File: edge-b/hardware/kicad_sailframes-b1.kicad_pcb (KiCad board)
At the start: 2 copper layers, 80 x 56 mm, 0 parts

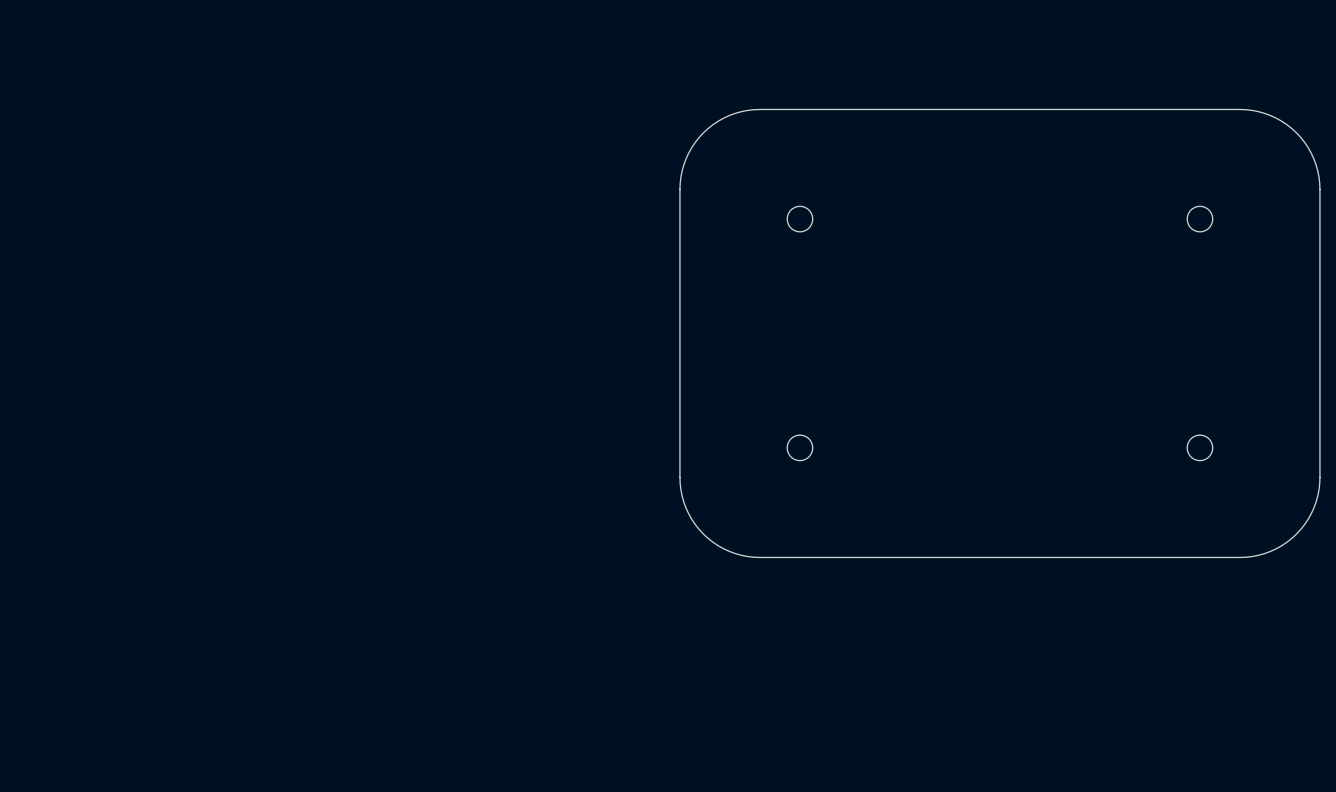
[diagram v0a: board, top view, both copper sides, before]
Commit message: B1 PCB v0.12: portrait rounded rectangle with top+bottom cut for expansion space
Final PCB outline:
- 79.3 x 73.9 mm rounded rectangle (R.377 on all 4 corners)
- Top and bottom cut symmetrically from original 104.7 mm Polycase template,
  leaving ~15.4 mm clear at each end for future expansion PCBs (GNSS antenna
  above the main PCB; spare module space below)
- 4 mounting holes at 2.375" (60.325 mm) X spacing, page-6 inner Y heights:
    (109.49, 76.97), (169.81, 76.97), (109.49, 126.98), (169.81, 126.98)
- Discards the page-6 corner-ear/cutout features since cuts remove the
  corners; portrait orientation matches installed pose (long axis vertical)

Co-Authored-By: Claude Opus 4.7 (1M context) <noreply@anthropic.com>
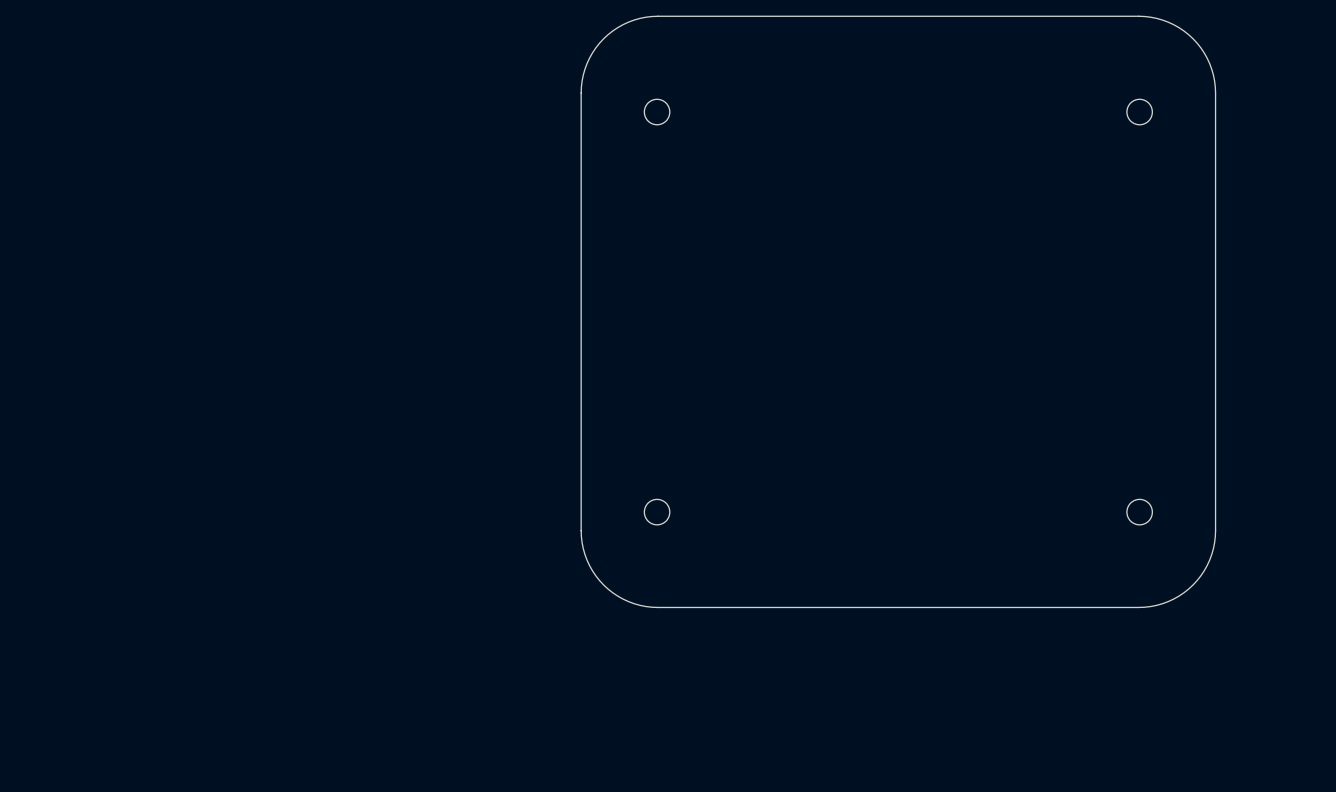
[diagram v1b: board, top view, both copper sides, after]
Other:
- board size 80 x 56 mm -> 79.3 x 73.9 mm
- board text added: "B1 PCB outline v0.5 — full Polycase ML-34BF-PCB template Envelope: 104.7 x 79.3 mm with 4x R.377 (9.6 mm) outer corners 4 edge notches centered on each side (R.125 / 3.18 mm inside fillets) Top/bottom notches: 73.9 mm wide x 9.6 mm deep Left/right notches: 46.6 mm wide x 9.6 mm deep 8 mounting holes NPTH 3.18 mm: 4 outer @ 85 x 60.3 mm, 4 inner @ 50 x 28.6 mm GNSS antenna NOT on main PCB (separat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"
- board text removed: "B1 PCB outline v0.4 — Option B: small centered rectangle 80 x 56 mm centered on Polycase interior, R=10 mm corner fillets 4 mounting holes NPTH 3.18 mm at +/-(25, 14.3) mm from Polycase center (inner PCB-mounting boss positions, 50 x 28.6 mm pattern) Clears 4 corner brass-insert towers laterally (no cover-screw holes through PCB) Cover screws engage corner brass inserts independently of PCB Anten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"

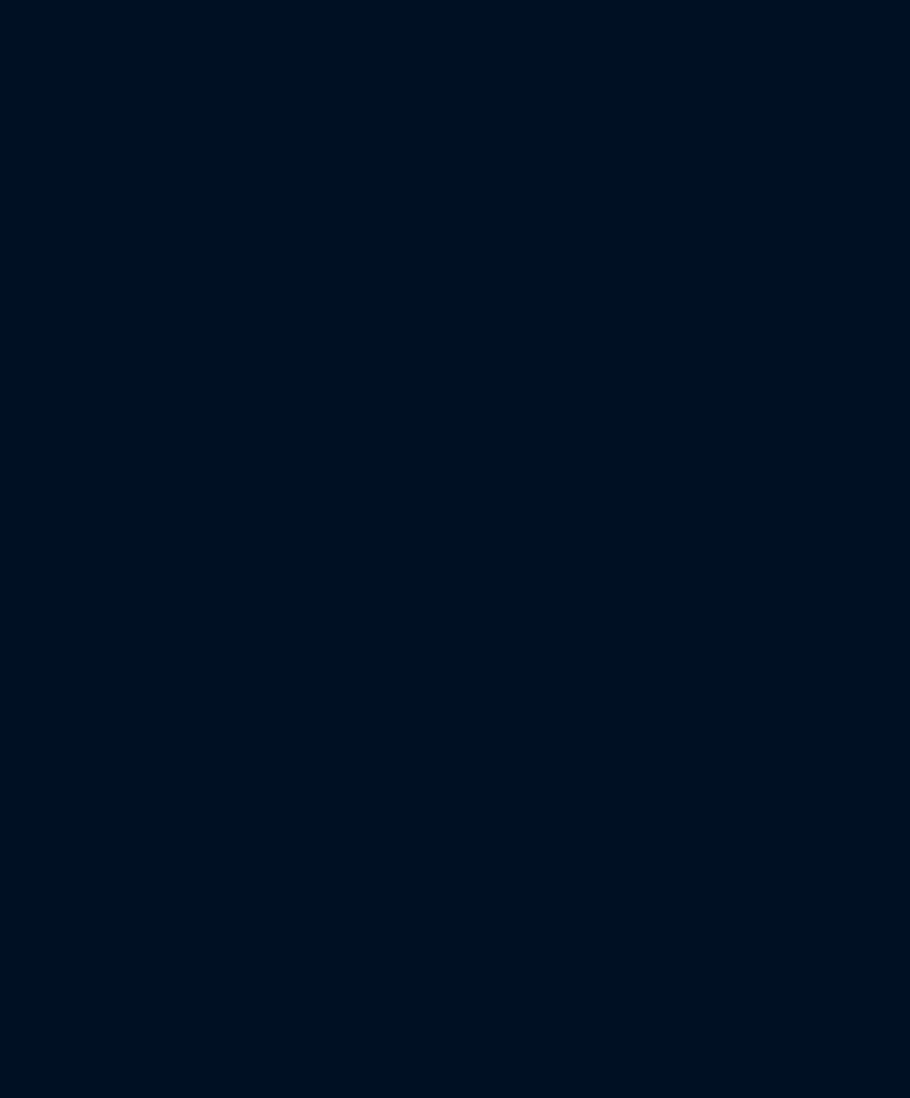
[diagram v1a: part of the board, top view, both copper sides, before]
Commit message: B1 schematic: fix pull-up topology bugs + ERC clean
Schematic fixes:
- Redrew R21/R22 I2C pull-ups as parallel topology (was chained series,
  shorting V3V3 to I2C_SDA/SCL)
- Redrew R23-R27 SD pull-ups as parallel topology (was chained series,
  shorting V3V3 to HSPI_CS/MOSI/MISO/SCK/SD_CD — would have destroyed
  the ESP32 once 3V3 hit GPIO5 through R23)
- Redrew C12-C16 V3V3 decap caps as parallel from V3V3 rail to GND
  (was chained, same merging issue)
- Changed TP4056 (U2) footprint from SOIC-8 to SOIC-8-1EP_3.9x4.9mm
  to expose pad 9 (thermal pad → GND)
- Deleted 2 dangling wire stubs near TP4056 and LATCH_Q_RB

ERC clean: 0 errors, 0 warnings. Cosmetic checks suppressed in project
settings (off-grid endpoints, Unspecified pin-type combinations, etc.).

PCB: F8 sync pulled in all 50 footprints; netlist now correct.

Co-Authored-By: Claude Opus 4.7 (1M context) <noreply@anthropic.com>
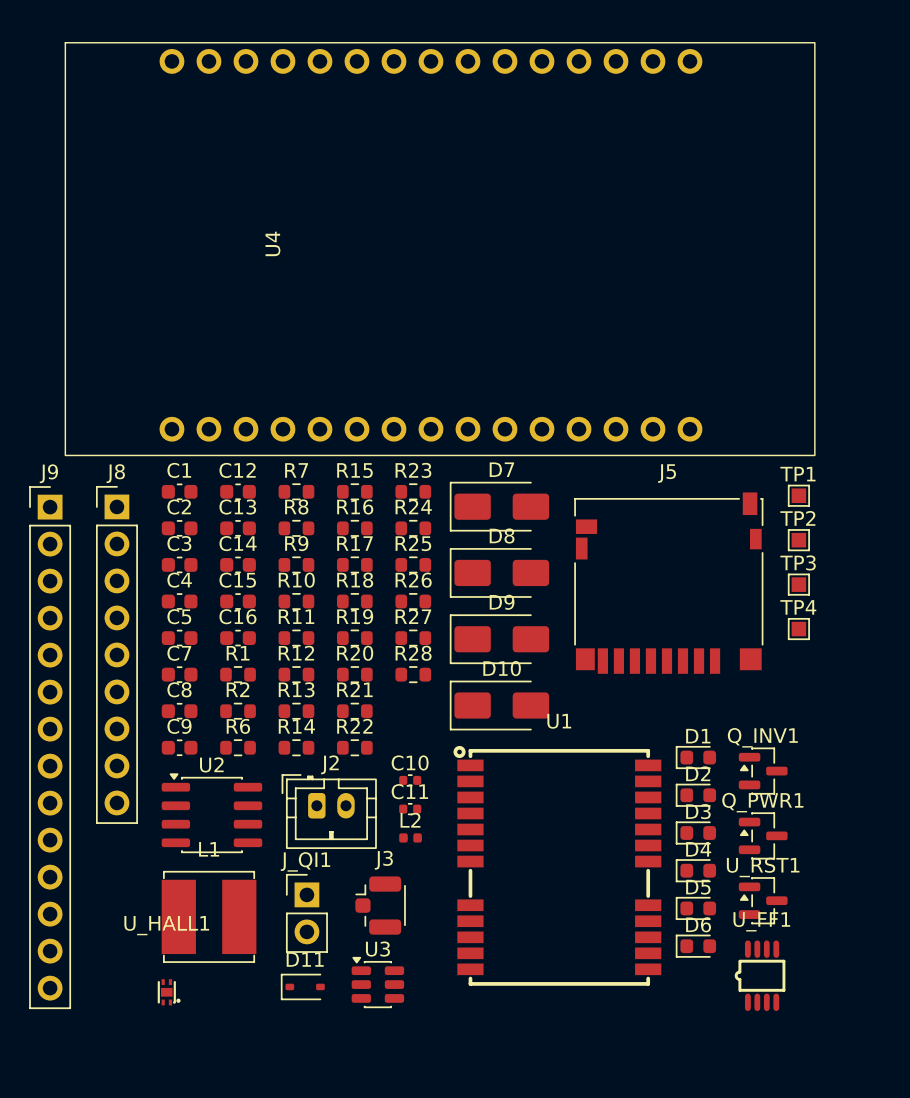
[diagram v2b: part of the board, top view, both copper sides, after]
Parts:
- added C1: 100nF, Capacitor_SMD:C_0603_1608Metric, F.Cu at (39.7, 96.7)
- added C10: 10nF, Capacitor_SMD:C_0402_1005Metric, F.Cu at (55.5, 116.5)
- added C11: 100pF, Capacitor_SMD:C_0402_1005Metric, F.Cu at (55.5, 118.5)
- added C12: 10uF, Capacitor_SMD:C_0603_1608Metric, F.Cu at (43.7, 96.7)
- added C13: 100nF, Capacitor_SMD:C_0603_1608Metric, F.Cu at (43.7, 99.2)
- added C14: 10nF, Capacitor_SMD:C_0603_1608Metric, F.Cu at (43.7, 101.8)
- added C15: 10uF, Capacitor_SMD:C_0603_1608Metric, F.Cu at (43.7, 104.3)
- added C16: 100nF, Capacitor_SMD:C_0603_1608Metric, F.Cu at (43.7, 106.8)
- added C2: 10uF, Capacitor_SMD:C_0603_1608Metric, F.Cu at (39.7, 99.2)
- added C3: 100nF, Capacitor_SMD:C_0603_1608Metric, F.Cu at (39.7, 101.8)
- added C4: 10uF, Capacitor_SMD:C_0603_1608Metric, F.Cu at (39.7, 104.3)
- added C5: 100nF, Capacitor_SMD:C_0603_1608Metric, F.Cu at (39.7, 106.8)
- added C7: 10uF, Capacitor_SMD:C_0603_1608Metric, F.Cu at (39.7, 109.3)
- added C8: 22uF, Capacitor_SMD:C_0603_1608Metric, F.Cu at (39.7, 111.8)
- added C9: 100nF, Capacitor_SMD:C_0603_1608Metric, F.Cu at (39.7, 114.3)
- added D1: BLUE, LED_SMD:LED_0603_1608Metric, F.Cu at (75.3, 115.0)
- added D10: SS14, Diode_SMD:D_SMA, F.Cu at (61.8, 111.4)
- added D11: BAT54, Diode_SMD:D_SOD-323, F.Cu at (48.3, 130.7)
- added D2: YELLOW, LED_SMD:LED_0603_1608Metric, F.Cu at (75.3, 117.6)
- added D3: GREEN, LED_SMD:LED_0603_1608Metric, F.Cu at (75.3, 120.2)
- added D4: RED, LED_SMD:LED_0603_1608Metric, F.Cu at (75.3, 122.7)
- added D5: WHITE, LED_SMD:LED_0603_1608Metric, F.Cu at (75.3, 125.3)
- added D6: CYAN, LED_SMD:LED_0603_1608Metric, F.Cu at (75.3, 127.9)
- added D7: SS14, Diode_SMD:D_SMA, F.Cu at (61.8, 97.8)
- added D8: SS14, Diode_SMD:D_SMA, F.Cu at (61.8, 102.3)
- added D9: SS14, Diode_SMD:D_SMA, F.Cu at (61.8, 106.9)
- added J2: JST_PH_BAT, Connector_JST:JST_PH_B2B-PH-K_1x02_P2.00mm_Vertical, F.Cu at (49.1, 118.3)
- added J3: U.FL, Connector_Coaxial:U.FL_Hirose_U.FL-R-SMT-1_Vertical, F.Cu at (53.8, 125.1)
- added J5: MICROSD, Connector_Card:microSD_HC_Hirose_DM3D-SF, F.Cu at (73.3, 103.0)
- added J8: BNO085_SOCKET, Connector_PinHeader_2.54mm:PinHeader_1x09_P2.54mm_Vertical, F.Cu at (35.4, 97.8)
- added J9: HOSYOND_3.5_TFT, Connector_PinHeader_2.54mm:PinHeader_1x14_P2.54mm_Vertical, F.Cu at (30.8, 97.8)
- added J_QI1: QI_PADS, Connector_PinHeader_2.54mm:PinHeader_1x02_P2.54mm_Vertical, F.Cu at (48.4, 124.4)
- added L1: 22uH, Inductor_SMD:L_Bourns_SRN6045TA, F.Cu at (41.7, 125.9)
- added L2: 33nH, Inductor_SMD:L_0402_1005Metric, F.Cu at (55.5, 120.5)
- added Q_INV1: 2N3904, Package_TO_SOT_SMD:SOT-23, F.Cu at (79.7, 115.9)
- added Q_PWR1: AO3401A, Package_TO_SOT_SMD:SOT-23, F.Cu at (79.7, 120.4)
- added R1: 100k, Resistor_SMD:R_0603_1608Metric, F.Cu at (43.7, 109.3)
- added R10: 100k, Resistor_SMD:R_0603_1608Metric, F.Cu at (47.7, 104.3)
- added R11: 13.7k, Resistor_SMD:R_0603_1608Metric, F.Cu at (47.7, 106.8)
- added R12: 100k, Resistor_SMD:R_0603_1608Metric, F.Cu at (47.7, 109.3)
- added R13: 10k, Resistor_SMD:R_0603_1608Metric, F.Cu at (47.7, 111.8)
- added R14: 10k, Resistor_SMD:R_0603_1608Metric, F.Cu at (47.7, 114.3)
- added R15: 100k, Resistor_SMD:R_0603_1608Metric, F.Cu at (51.7, 96.7)
- added R16: 10k, Resistor_SMD:R_0603_1608Metric, F.Cu at (51.7, 99.2)
- added R17: 220, Resistor_SMD:R_0603_1608Metric, F.Cu at (51.7, 101.8)
- added R18: 220, Resistor_SMD:R_0603_1608Metric, F.Cu at (51.7, 104.3)
- added R19: 220, Resistor_SMD:R_0603_1608Metric, F.Cu at (51.7, 106.8)
- added R2: 100k, Resistor_SMD:R_0603_1608Metric, F.Cu at (43.7, 111.8)
- added R20: 470, Resistor_SMD:R_0603_1608Metric, F.Cu at (51.7, 109.3)
- added R21: 4.7k, Resistor_SMD:R_0603_1608Metric, F.Cu at (51.7, 111.8)
- added R22: 4.7k, Resistor_SMD:R_0603_1608Metric, F.Cu at (51.7, 114.3)
- added R23: 10k, Resistor_SMD:R_0603_1608Metric, F.Cu at (55.7, 96.7)
- added R24: 10k, Resistor_SMD:R_0603_1608Metric, F.Cu at (55.7, 99.2)
- added R25: 10k, Resistor_SMD:R_0603_1608Metric, F.Cu at (55.7, 101.8)
- added R26: 10k, Resistor_SMD:R_0603_1608Metric, F.Cu at (55.7, 104.3)
- added R27: 10k, Resistor_SMD:R_0603_1608Metric, F.Cu at (55.7, 106.8)
- added R28: 10k, Resistor_SMD:R_0603_1608Metric, F.Cu at (55.7, 109.3)
- added R6: 2k, Resistor_SMD:R_0603_1608Metric, F.Cu at (43.7, 114.3)
- added R7: 10k, Resistor_SMD:R_0603_1608Metric, F.Cu at (47.7, 96.7)
- added R8: 1k, Resistor_SMD:R_0603_1608Metric, F.Cu at (47.7, 99.2)
- added R9: 1k, Resistor_SMD:R_0603_1608Metric, F.Cu at (47.7, 101.8)
- added TP1: GNSS_TXD, TestPoint:TestPoint_Pad_1.0x1.0mm, F.Cu at (82.2, 97.0)
- added TP2: GNSS_RXD, TestPoint:TestPoint_Pad_1.0x1.0mm, F.Cu at (82.2, 100.1)
- added TP3: GNSS_RESET_N, TestPoint:TestPoint_Pad_1.0x1.0mm, F.Cu at (82.2, 103.1)
- added TP4: GND, TestPoint:TestPoint_Pad_1.0x1.0mm, F.Cu at (82.2, 106.2)
- added U1: LC29HEAMD, B1_JLC:GPSM-SMD_24P-L16.0-W12.2-P1.10-TL, F.Cu at (65.8, 122.5)
- added U2: TP4056, Package_SO:SOIC-8_3.9x4.9mm_P1.27mm, F.Cu at (41.9, 118.9)
- added U3: MT3608, Package_TO_SOT_SMD:SOT-23-6, F.Cu at (53.3, 130.6)
- added U4: ESP32_DEVKIT_V1, b1_Library:ESP32DEVIKITV1, F.Cu at (39.2, 92.4)
- added U_FF1: SN74LVC1G74, B1_JLC:SM8_L3.0-W2.8-P0.65-LS4.0-BL, F.Cu at (79.7, 130.0)
- added U_HALL1: DRV5032AJ, B1_DRV5032AJ:X2SON-4_L1.1-W1.4-P0.50-BR-EP, F.Cu at (38.8, 131.1)
- added U_RST1: MAX809T, Package_TO_SOT_SMD:SOT-23, F.Cu at (79.7, 124.8)
